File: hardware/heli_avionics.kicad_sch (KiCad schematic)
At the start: 9 parts, among them J1 UPDI, SW1 Reset, U1 ATmega4808-A

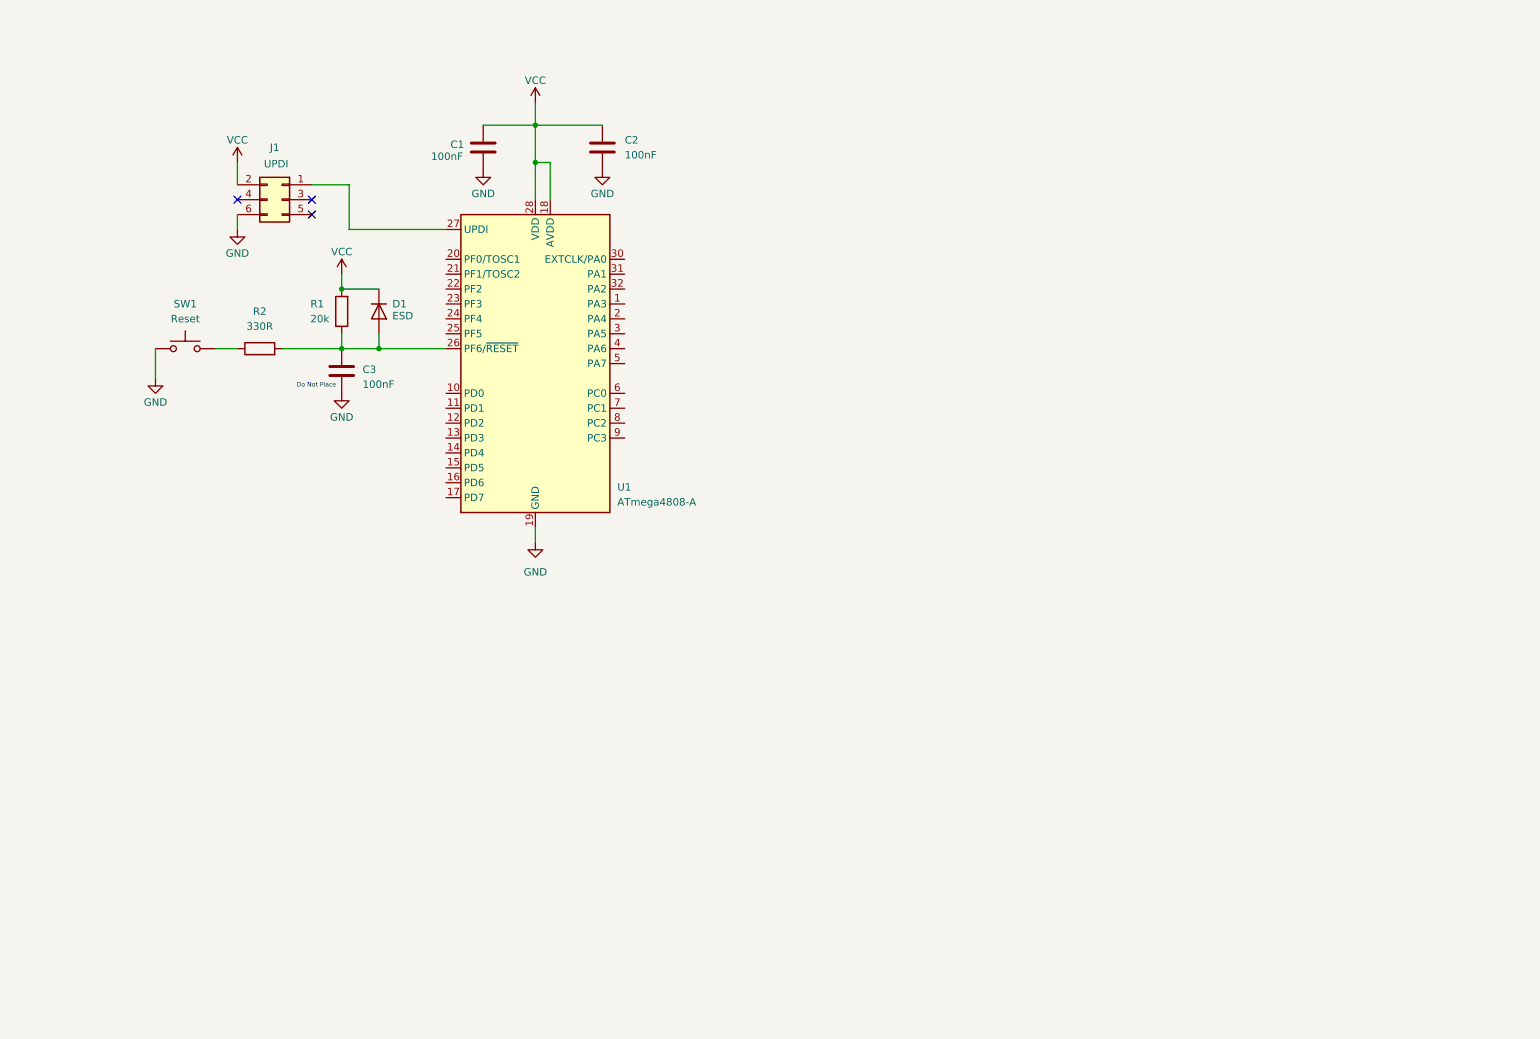
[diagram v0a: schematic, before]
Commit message: Added basic connections for nrf24
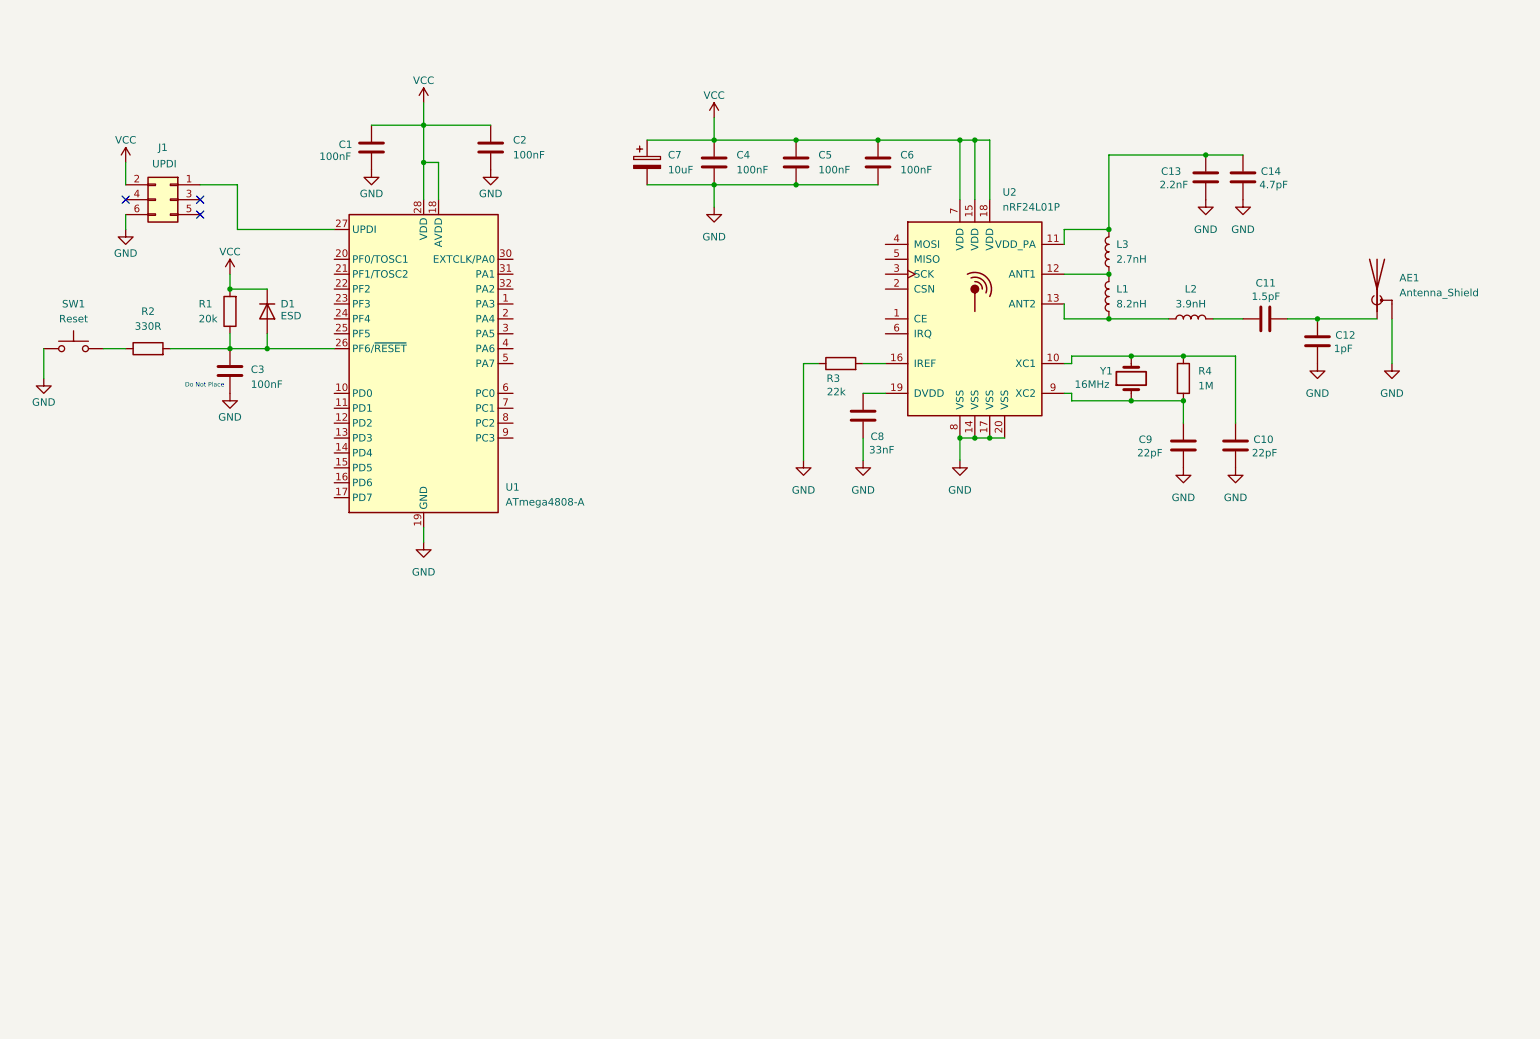
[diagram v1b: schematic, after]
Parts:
- added AE1: Antenna_Shield, symbol Device:Antenna_Shield
- added C10, C9: 22pF, symbol Device:C
- added C11: 1.5pF, symbol Device:C
- added C12: 1pF, symbol Device:C
- added C13: 2.2nF, symbol Device:C
- added C14: 4.7pF, symbol Device:C
- added C4, C5, C6: 100nF, symbol Device:C
- added C7: 10uF, symbol Device:C_Polarized
- added C8: 33nF, symbol Device:C
- added L1: 8.2nH, symbol Device:L
- added L2: 3.9nH, symbol Device:L
- added L3: 2.7nH, symbol Device:L
- added R3: 22k, symbol Device:R
- added R4: 1M, symbol Device:R
- added U2: nRF24L01P, Package_DFN_QFN:QFN-20-1EP_4x4mm_P0.5mm_EP2.5x2.5mm, symbol RF:nRF24L01P
- added Y1: 16MHz, symbol Device:Crystal
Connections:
- net GND: now also AE1.2 (Shield), C10.2, C12.2, C13.2, C14.2, C4.2, C5.2, C6.2, C7.2, C8.2, C9.2, R3.1, U2.14 (VSS), U2.17 (VSS), U2.20 (VSS), U2.8 (VSS)
- net VCC: now also C4.1, C5.1, C6.1, C7.1, U2.15 (VDD), U2.18 (VDD), U2.7 (VDD)
- new net: L1.1, L2.1, U2.13 (ANT2)
- new net: C11.1, L2.2
- new net: R3.2, U2.16 (IREF)
- new net: C13.1, C14.1, L3.2, U2.11 (VDD_PA)
- new net: C9.1, R4.2, U2.9 (XC2), Y1.1
- new net: L1.2, L3.1, U2.12 (ANT1)
- new net: C10.1, R4.1, U2.10 (XC1), Y1.2
- new net: AE1.1 (A), C11.2, C12.1
- new net: C8.1, U2.19 (DVDD)
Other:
- moved on the sheet: C1, C2, C3, D1, J1, R1, R2, SW1, U1

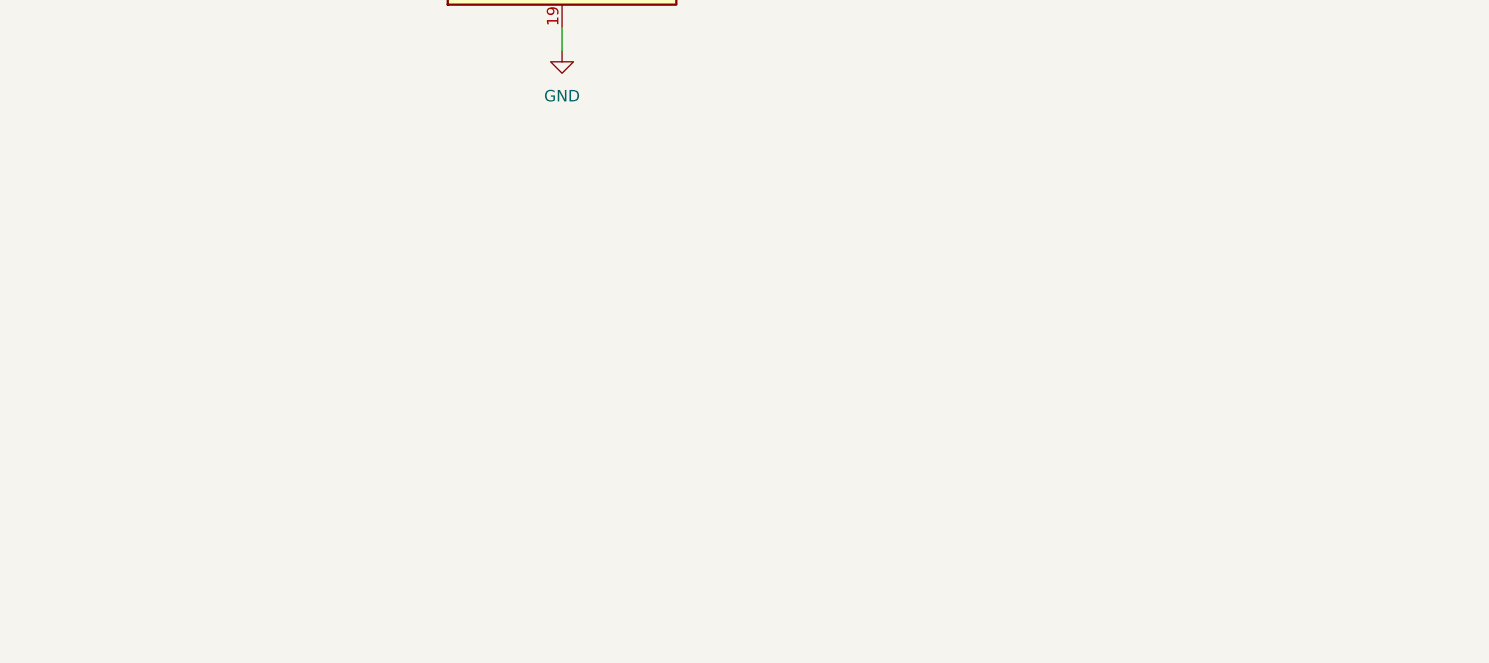
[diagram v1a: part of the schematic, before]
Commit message: Basic connections for motor drivers
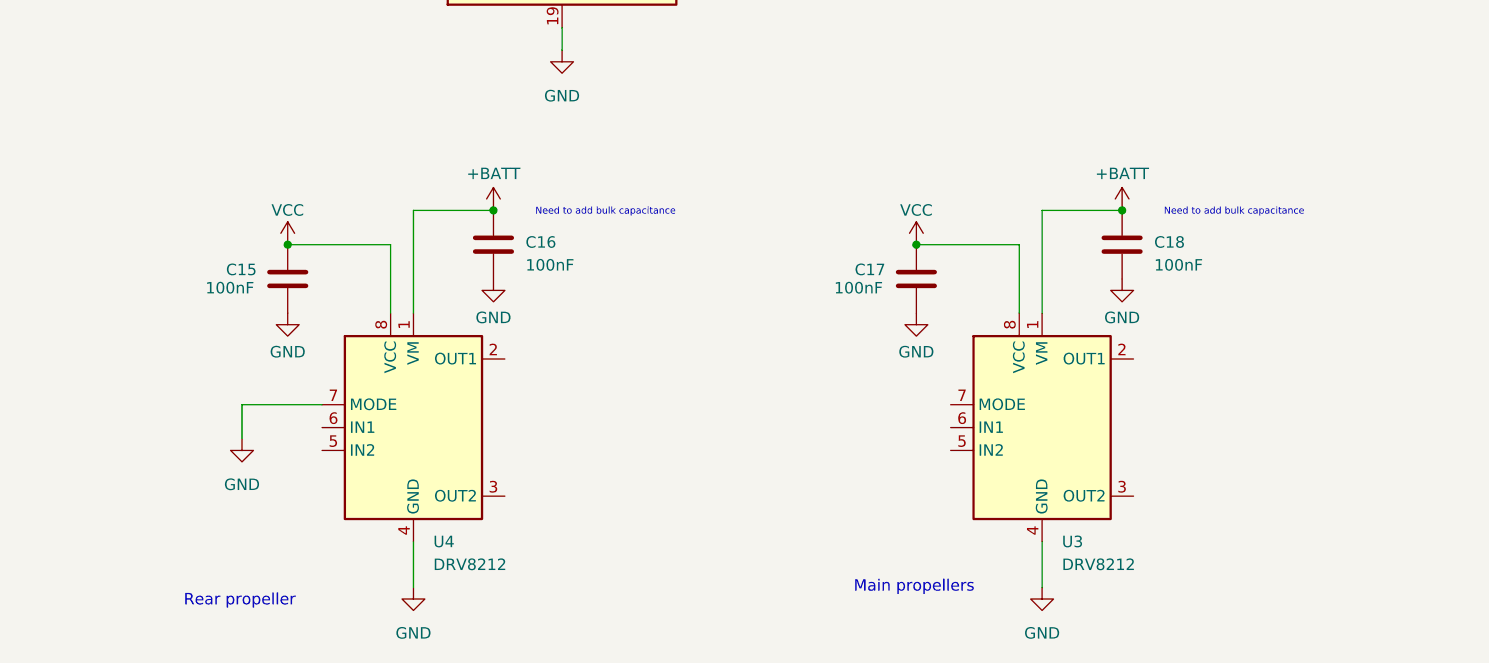
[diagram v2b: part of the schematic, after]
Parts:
- added C15, C16, C17, C18: 100nF, symbol Device:C
- added U3, U4: DRV8212, Package_SON:WSON-8-1EP_2x2mm_P0.5mm_EP0.9x1.6mm_ThermalVias, symbol heli_symbols:DRV8212
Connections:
- net GND: now also C15.2, C16.2, C17.2, C18.2, U3.4 (GND), U3.9 (GND), U4.4 (GND), U4.7 (MODE), U4.9 (GND)
- net VCC: now also C15.1, C17.1, U3.8 (VCC), U4.8 (VCC)
- new net +BATT: C16.1, C18.1, U3.1 (VM), U4.1 (VM)
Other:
- note added: "Main propellers"
- note added: "Need to add bulk capacitance"
- note added: "Rear propeller"

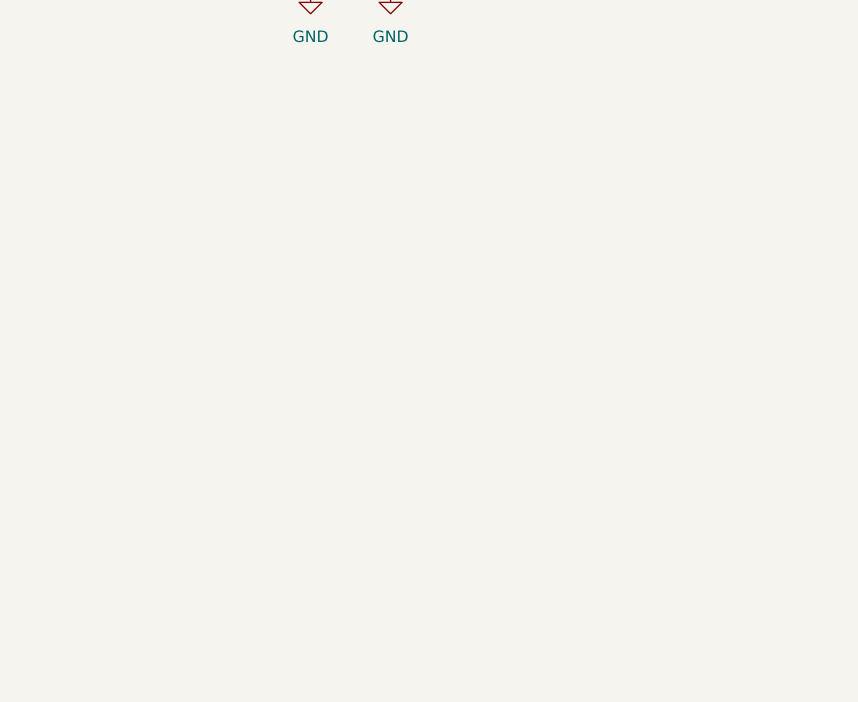
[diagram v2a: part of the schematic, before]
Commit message: Added basic connections for pressure sensor
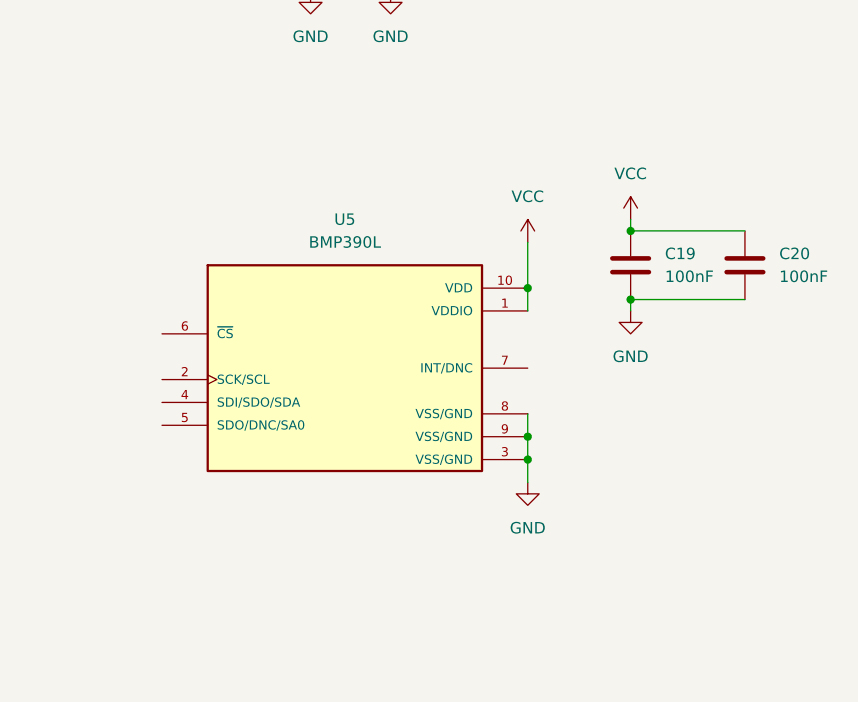
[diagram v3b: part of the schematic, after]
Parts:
- added C19, C20: 100nF, symbol Device:C
- added U5: BMP390L, heli-footprints:BMP390L, symbol heli_symbols:BMP390L
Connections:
- net GND: now also C19.2, C20.2, U5.3 (VSS/GND), U5.8 (VSS/GND), U5.9 (VSS/GND)
- net VCC: now also C19.1, C20.1, U5.1 (VDDIO), U5.10 (VDD)

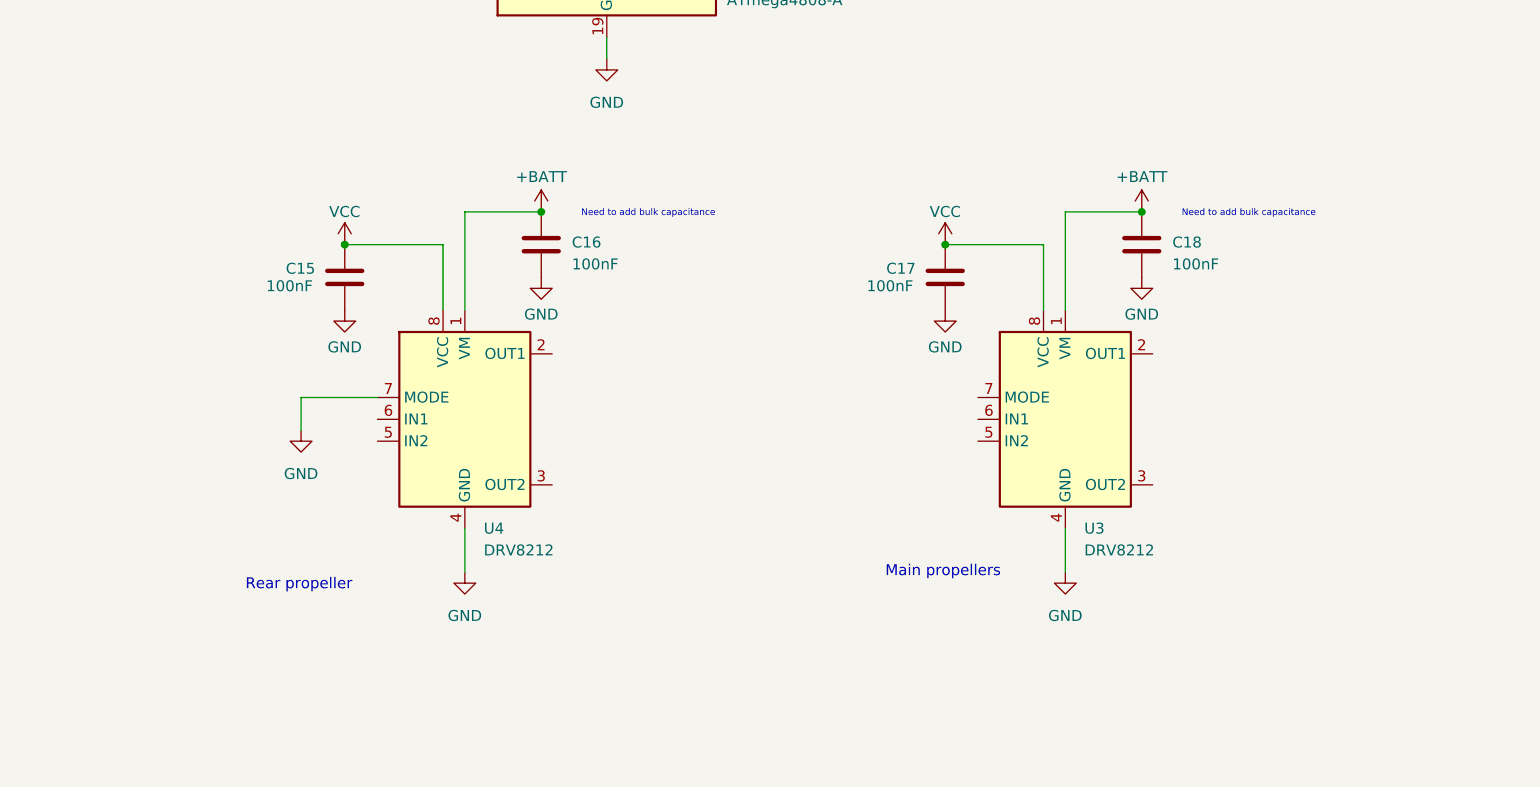
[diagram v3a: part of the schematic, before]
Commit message: Basic connections for voltage regulator
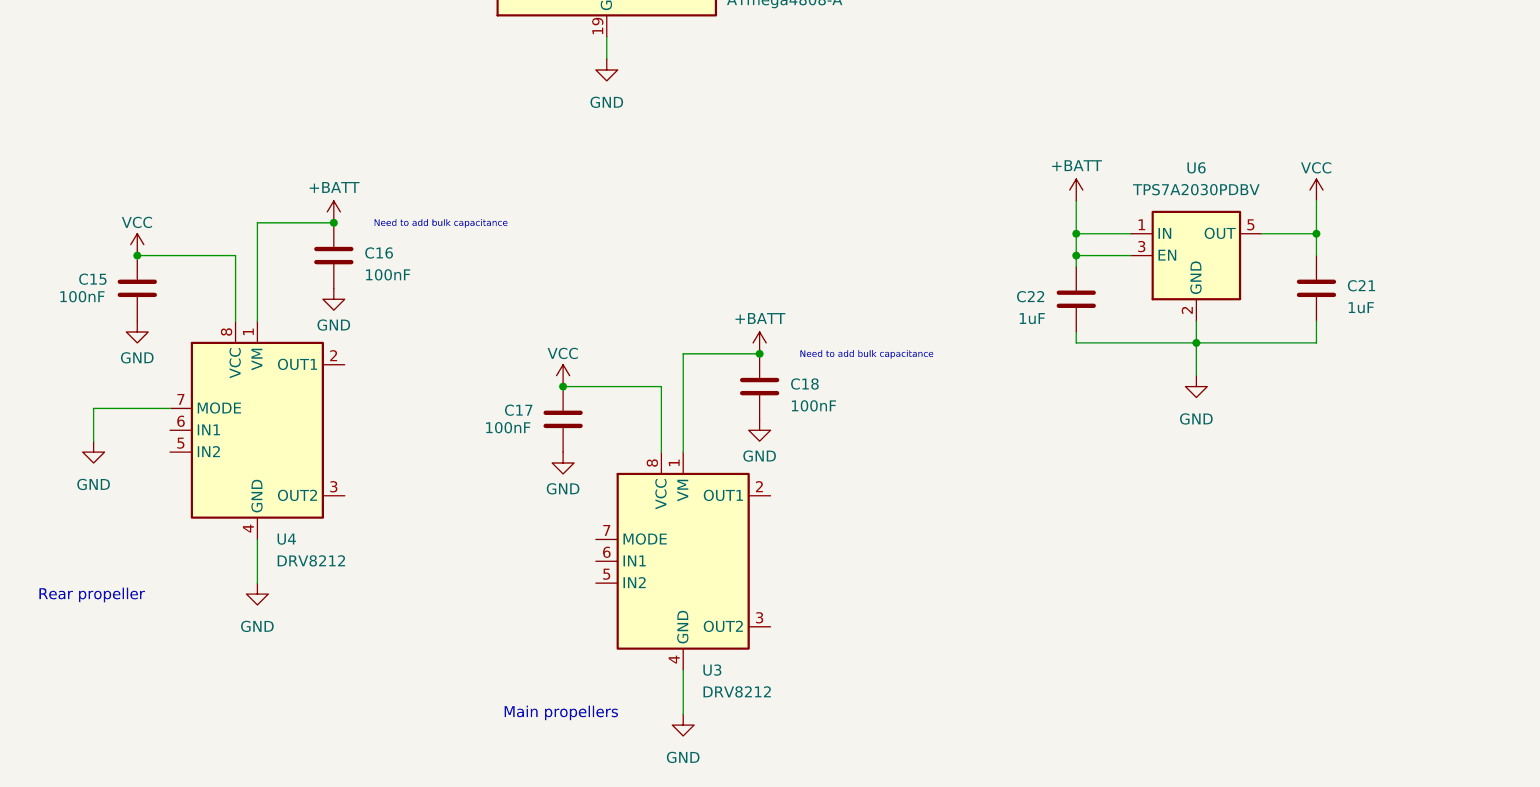
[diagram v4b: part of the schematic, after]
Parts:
- added C21, C22: 1uF, symbol Device:C
- added U6: TPS7A2030PDBV, Package_TO_SOT_SMD:SOT-23-5, symbol heli_symbols:TPS7A20
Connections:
- net +BATT: now also C22.1, U6.1 (IN), U6.3 (EN)
- net GND: now also C21.2, C22.2, U6.2 (GND)
- net VCC: now also C21.1, U6.5 (OUT)
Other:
- moved on the sheet: C15, C16, C17, C18, U3, U4
